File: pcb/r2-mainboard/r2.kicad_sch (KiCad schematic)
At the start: 0 parts

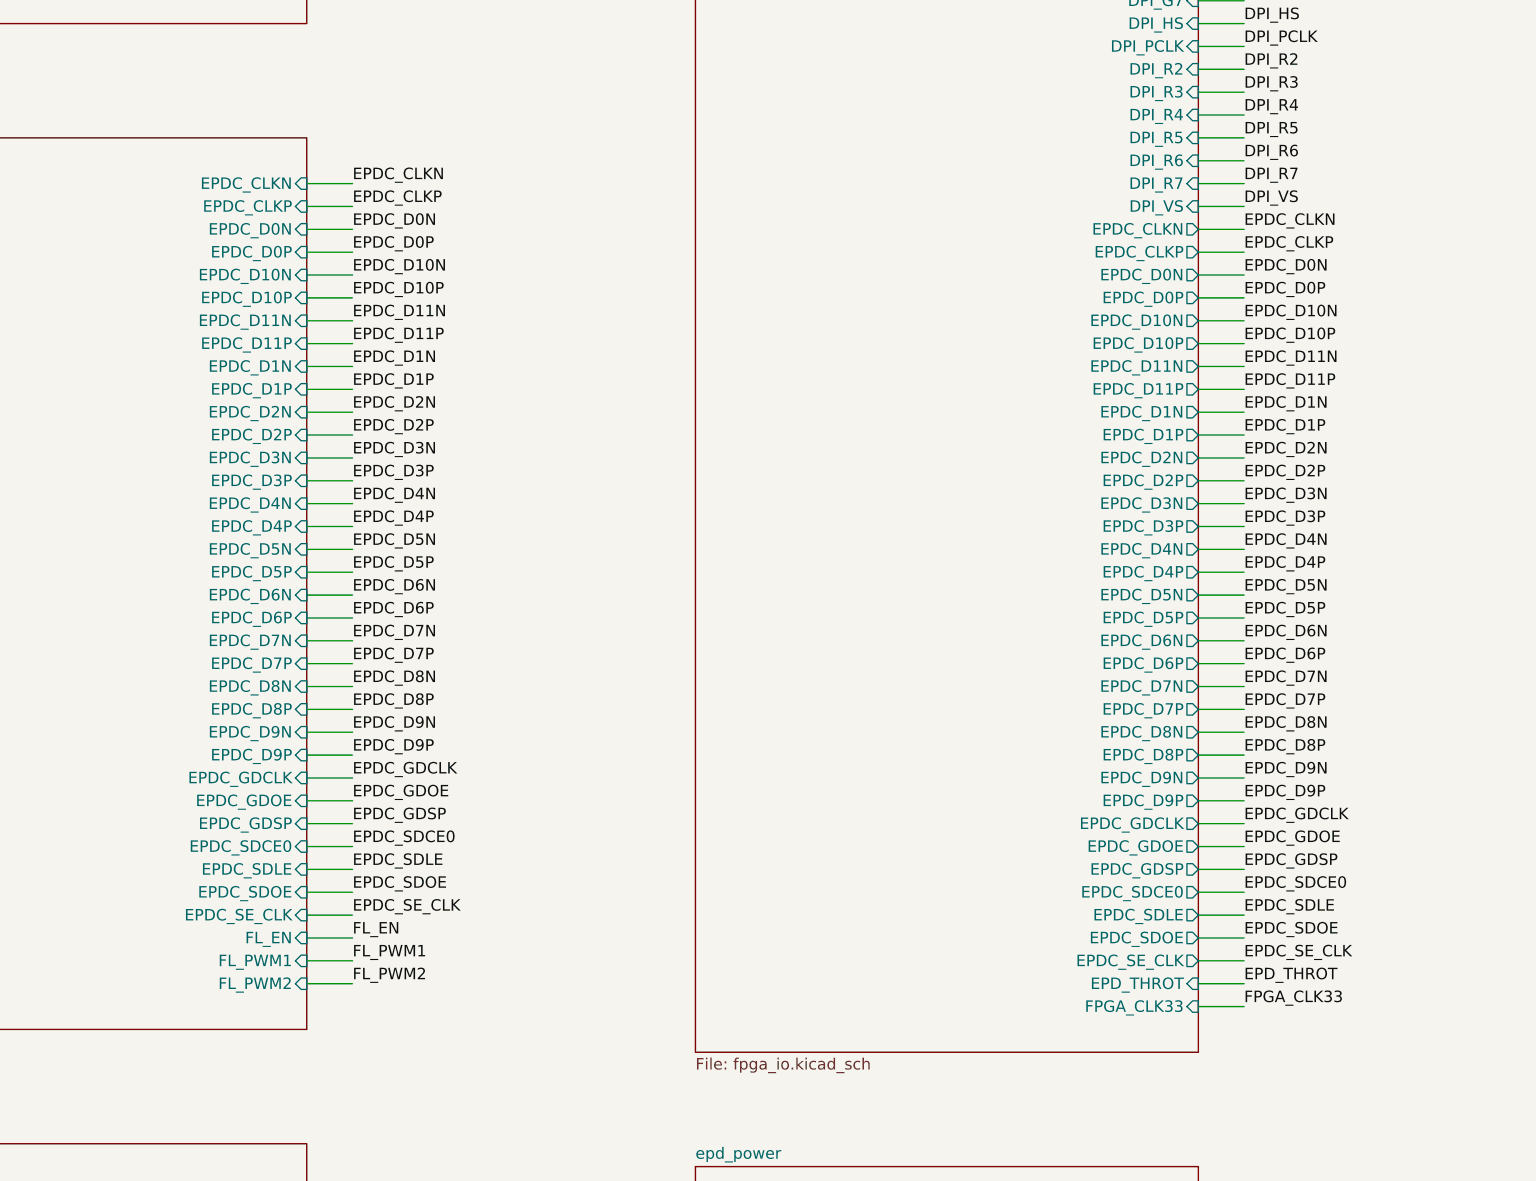
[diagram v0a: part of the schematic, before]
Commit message: R2: WP5 review answer 2 -- J3 is deleted, and with it ten dead nets
Owner's decision, manual-analysis/Analysis_fpga.md: "Yes, delete J3 connector."

J3 was the 16-pin panel connector. It carried nothing but EPDC_D8-D11 (eight
nets), EPDC_CLKP/CLKN and six grounds, and check_ucf.py had already shown that
no LOC line in Caster's constraint.ucf assigns any of the ten -- EPD_SD is 16
bits in every build variant and the UCF maps those 16 to panel pairs D0-D7, and
there is no EPD_CLK port in top.v at all. So this is not an unpopulated option;
nothing in the gateware could drive it.

Why it existed upstream, which the owner also asked: Glider is a general-purpose
EPD monitor. README "Screen Adapters" -- "A single 50pin connector is enough for
8/16-bit screens, the 16 pin connector additionally adds support for LVDS
screens and 32-bit/64-bit screens." In the screen list every MiniLVDS panel is
8" 1920x1440 or larger; every 6" 1448x1072 panel is TTL on 34 pins. R2 is a 6"
reader, so J3 is the large-panel option and J6 alone is the reader's connector.

tools/patch_drop_j3.py does it surgically -- both sheets are frozen. On epd:
J3, #PWR0201, ten hierarchical labels, ten signal wires, the thirteen-wire
ground comb and its six junctions. On fpga_io: ten labels and wires, and ten
no-connect flags on C7 A7 B8 A8 C9 A9 E7 E8 D8 C8. port_r1.py keeps the ten
names in HIER so a --force re-port still reproduces R1, and subtracts a new
DEAD_ON_R2 set from the sheet-pin list instead.

Verified: netlist before/after is 351 nets either way -- exactly the ten dead
nets gone, exactly seven J3 nodes off GND, ten new one-pin unconnected- nets on
the expected balls, and every other net byte-identical. check_ucf.py still 113
constrained balls / 0 failures, and its "reserved but not driven" list falls
from 11 balls to 1 (EPD_THROT). ERC unchanged at 105 excluding library links.
Both pages and the root rendered and read.

The r2.kicad_sch diff is large because removing ten sheet pins moves every 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
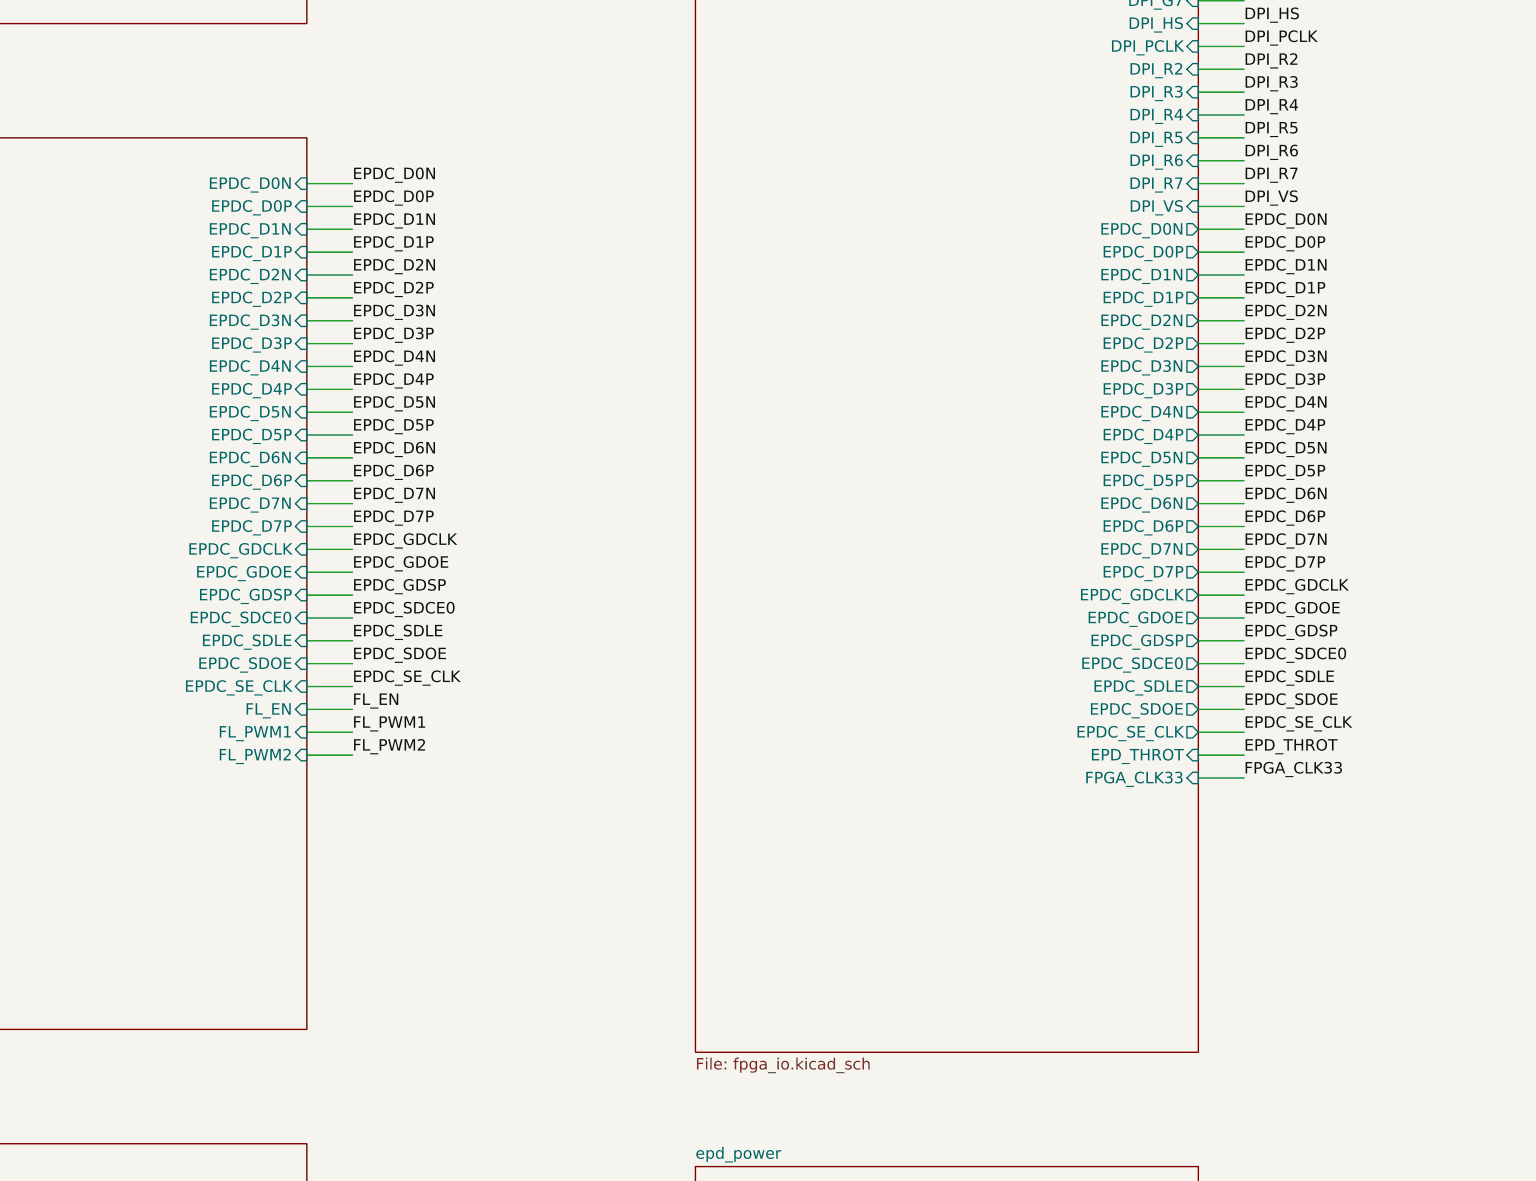
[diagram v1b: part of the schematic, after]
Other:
- sheet epd ports: added none; removed EPDC_CLKN, EPDC_CLKP, EPDC_D10N, EPDC_D10P, EPDC_D11N, EPDC_D11P, EPDC_D8N, EPDC_D8P, EPDC_D9N, EPDC_D9P
- sheet fpga_io ports: added none; removed EPDC_CLKN, EPDC_CLKP, EPDC_D10N, EPDC_D10P, EPDC_D11N, EPDC_D11P, EPDC_D8N, EPDC_D8P, EPDC_D9N, EPDC_D9P

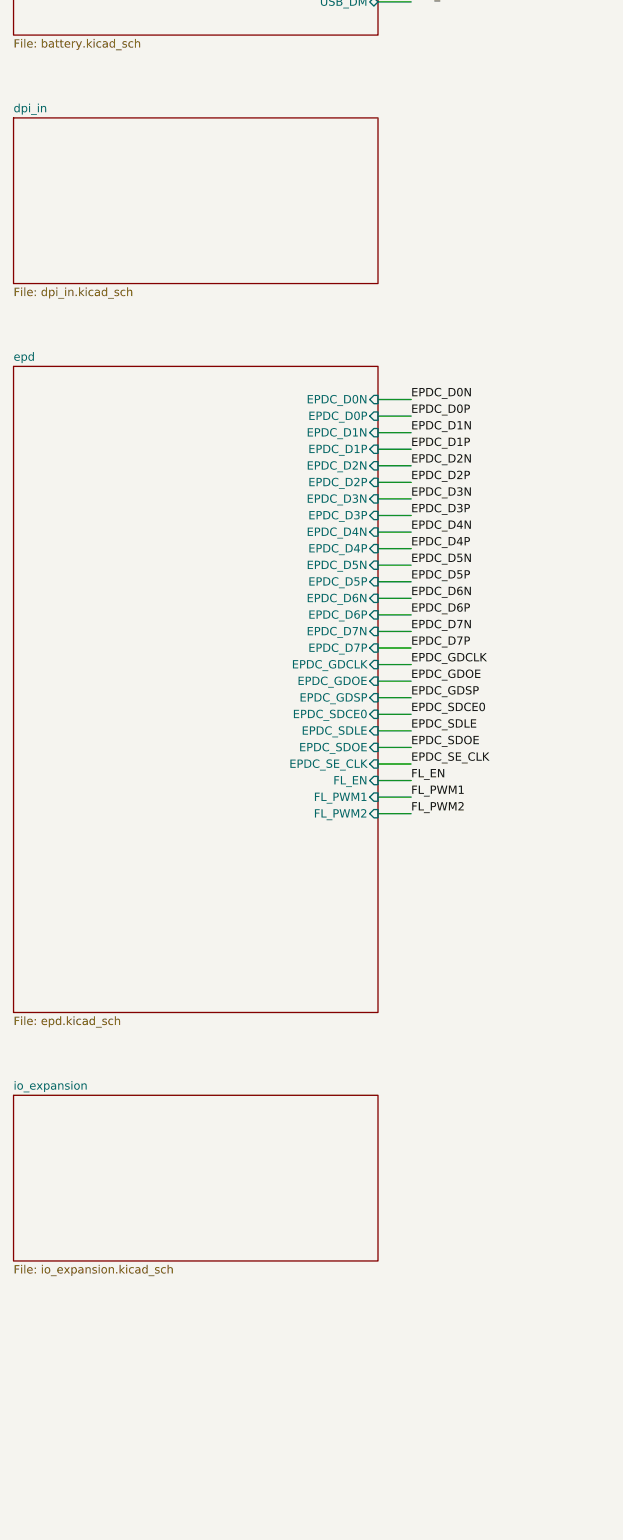
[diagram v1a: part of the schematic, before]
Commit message: R2: WP7 -- dpi_in drawn, and a silent short caught before it reached fab
tools/gen_dpi_in.py draws dpi_in.kicad_sch: unit 2 of the PCM-071, 22 pins
fanning into the 22 hierarchical labels fpga_io has exported since WP5. No
components at all, which is also how the "nothing may load DPI_R6/DPI_R7" rule
is satisfied -- a sheet note says so, so a later reviewer does not add the
"missing" termination.

The bit mapping is the whole content of the sheet and the only thing that can
be wrong in a way that still boots: VOUT0_DATA<n> = DPI_PIXEL[n], channel =
BGR[n/6], bit = 2 + n%6, where the 2 is RGB666 keeping the top six bits of each
channel. Verified three ways -- the generator asserts the 22 net names are
exactly the expected set with no duplicates and that D2/D4 land on R6/R7; every
claimed pin is re-read from som_pinout.json; and the exported netlist is
cross-checked against Caster's own UCF, where all 18 DPI_PIXEL LOC constraints
land on the ball the schematic wires.

A REAL BUG, found by that netlist check and not by ERC. set_sheet_pins grew
dpi_in's root box from 25.4 mm to 63.5 mm to fit 22 pins, and the taller box
swallowed epd's. wire_root's stubs then landed inside epd's box and merged the
two sheets' nets: seven DPI_* nets came out shorted to the panel bus, so
DPI_R2 was the same net as EPDC_D0N, with J6.38 and a second U41 ball on it.
The schematic stayed perfectly legal and ERC said nothing.

This is the *second* time -- WP5 lost seven FPGA balls to VCOM_MEA_EN the same
way when fpga_io grew. The guard existed but lived in layout_root.py, which
nothing was obliged to call. Moved: layout_root.overlaps()/assert_no_overlap()
are now the shared implementation, and wire_root.py calls it before emitting
anything. wire_root is the right home because it is what turns sheet pins into
nets, so it is the last place the check can prevent the short rather than
report it afterwards. Confirmed the guard fires on the broken tree, then
layout_root re-packed the column and eve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
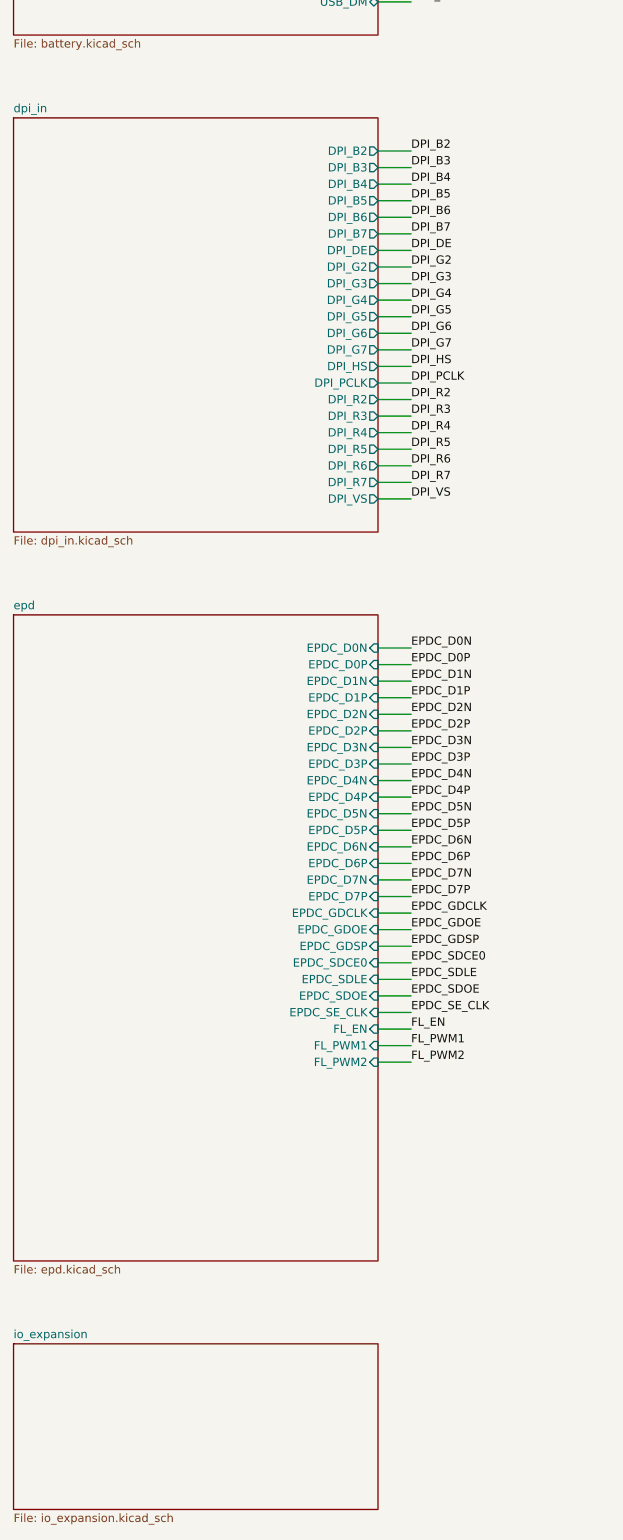
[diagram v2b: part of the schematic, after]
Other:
- sheet dpi_in ports: added DPI_B2, DPI_B3, DPI_B4, DPI_B5, DPI_B6, DPI_B7, DPI_DE, DPI_G2, DPI_G3, DPI_G4, DPI_G5, DPI_G6, DPI_G7, DPI_HS, DPI_PCLK, DPI_R2, DPI_R3, DPI_R4, DPI_R5, DPI_R6, DPI_R7, DPI_VS; removed none
